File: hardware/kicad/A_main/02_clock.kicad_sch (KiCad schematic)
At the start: 29 parts, among them U15 ADCLK846BCPZ, U16 SN65LVDS2DBVR, U17 SN65LVDS2DBVR, U18 SN65LVDS2DBVR, Y10 ABLNO-V-80.000MHZ

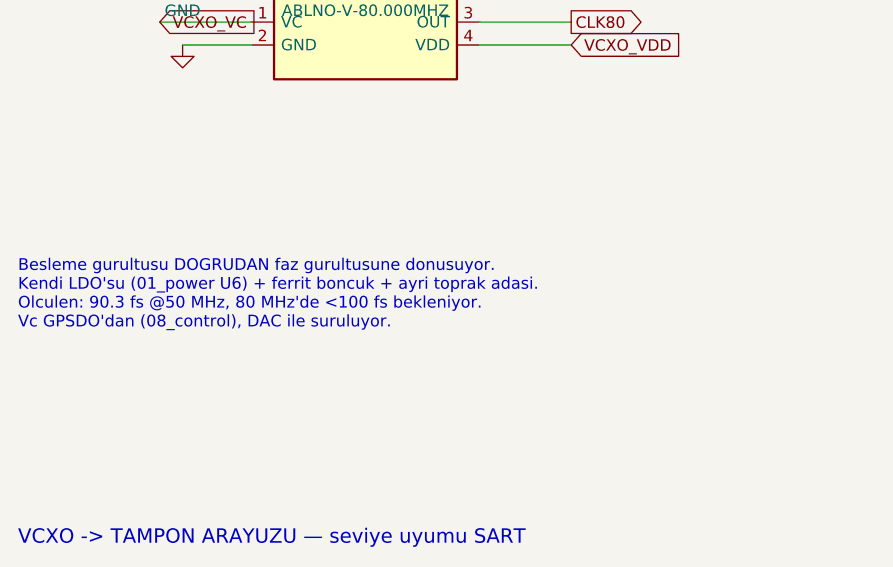
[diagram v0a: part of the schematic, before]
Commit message: Name the copyright holder and stamp it into the generated files
The repository had three licence files and no statement of who owns
the work. The only record of authorship was the git author field.

Copyleft depends on that statement. GPL and CERN-OHL-S work because
the holder grants permission on condition of reciprocity; with no
holder named there is nobody to require it from a downstream user.
Naming the author keeps the design open rather than closing it.

kicad/telif.py is the single source. The line reaches the schematics
through their title block and not through the generators, because
every schematic file is rewritten on each build and a header placed in
a generator would disappear at the first regeneration. All 23
schematics carry it. 109 source files have SPDX headers, split by the
project's own table: generators and the layout chain are hardware
under CERN-OHL-S-2.0, HDL and the audit tools are software under
GPL-3.0-only.

Board C's inductors also move to footprints that match parts that can
be bought. All of them sat on 0805 pads. Of the values this design
needs, 33 to 220 nH are 0603 parts, 470 and 820 nH are 0805, and
everything from 1000 nH upward is 1210, which is 3.2 by 2.5 mm and
does not fit an 0805 land. 32 inductors could not have been soldered.

A symbol-against-footprint check cannot find this. Those two agreed
with each other; what was wrong was the body size of the real part
behind the footprint.
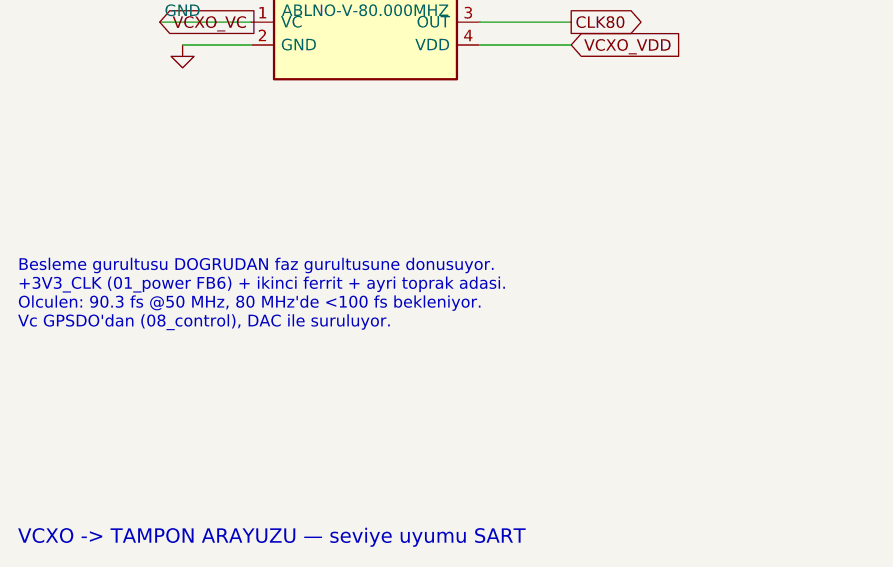
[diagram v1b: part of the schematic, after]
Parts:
- removed C210 (x2), C211 (x2): 100nF, Capacitor_SMD:C_0603_1608Metric, symbol Device:C
- added C210 (x2), C211 (x2): 100nF, Capacitor_SMD:C_0603_1608Metric, symbol Device:C
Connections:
- net +3V3: now also C210.1, C211.1
- net BUFCLK_N: now also C211.1
- net BUFCLK_P: now also C210.2
- net CLK80_DIV: now also C210.1
- net GND: now also C210.2, C211.2, C211.2
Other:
- note added: "Besleme gurultusu DOGRUDAN faz gurultusune donusuyor. +3V3_CLK (01_power FB6) + ikinci ferrit + ayri toprak adasi. Olculen: 90.3 fs @50 MHz, 80 MHz'de <100 fs bekleniyor. Vc GPSDO'dan (08_control), DAC ile suruluyor."
- note removed: "Besleme gurultusu DOGRUDAN faz gurultusune donusuyor. Kendi LDO'su (01_power U6) + ferrit boncuk + ayri toprak adasi. Olculen: 90.3 fs @50 MHz, 80 MHz'de <100 fs bekleniyor. Vc GPSDO'dan (08_control), DAC ile suruluyor."

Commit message: Correct the transmit envelope and add a third zero on 15 m to 10 m
The unit has no reconstruction filter. A comment on board A said that
the filter is on board C. Board C has no such filter: the transmit
signal enters through an SMA connector and goes to the transmit and
receive relay. The datasheet also gave a cutoff frequency for this
filter that does not exist.

A sampling DAC does not make one frequency. It makes images at
|k*fs +/- fd|. The zero-order hold gives each image a different
level, and the function falls slowly. If the carrier is near Nyquist,
an image at a lower frequency can be stronger than the carrier.

A new tool measures this. It uses the harmonic filter of board D,
because that filter is the only one in the transmit path.

  15 m to 10 m   4-channel   image at 10.3 MHz is 10.4 dB stronger
  6 m            4-channel   image is 14.2 dB stronger
  6 m            2-channel   image is 7.4 dB stronger
  20 m, 17 m     4-channel   -12.0 dBc, the limit is -43 dBc
  15 m to 10 m   2-channel   -40.4 dBc, the limit is -43 dBc

Only the last one is correctable.

That filter position must attenuate three frequencies: 42 MHz (the
second harmonic of 21 MHz), 63 MHz (the third harmonic) and 50.3 MHz
(the DAC image). A five-pole filter has two traps. No pair of trap
frequencies gives more than 1.9 dB of margin, and 1.9 dB is not a
margin: one E24 rounding already cost 19 dB in this project.

A shunt series-LC at the output adds a third zero. The image goes
from -40.4 dBc to -47.3 dBc, and the margin becomes 23 dB. Above
resonance the branch is capacitive and attenuates the whole stopband,
so the harmonics also improve. The passband loss falls from 1.35 dB
to 0.99 dB.

The transmit envelope is now written honestly. The RTL said "Nyquist
is 20 MHz, so 160 m to 17 m". Nyquist alone is not enough: the images
must also be filtered, and the real limit is lower.

  4-channel   160 m to 30 m
  2-channel   160 m to 10 m
  6 m         no transmit. Receive works, with 68 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
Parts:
- removed C210 (x2), C211 (x2): 100nF, Capacitor_SMD:C_0603_1608Metric, symbol Device:C
- added C210 (x2), C211 (x2): 100nF, Capacitor_SMD:C_0603_1608Metric, symbol Device:C
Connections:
- net +3V3: now also C210.1, C211.1
- net BUFCLK_N: now also C211.1
- net BUFCLK_P: now also C210.2
- net CLK80_DIV: now also C210.1
- net GND: now also C210.2, C211.2, C211.2

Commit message: Add bulk capacitors to the 1.8 V rails and measure the supply network
Counting decoupling capacitors is not enough. The existing check asks
whether each supply pin has a capacitor. That is necessary but not
sufficient. What matters is the impedance that the chip sees on the
rail, against frequency. No connectivity check can see this: the
schematic is correct, the netlist is correct, the DRC is clean, and
the rail still rings.

The +1V8 rail and the +1V8_D rail had no bulk capacitor. The largest
part was 1 uF. The regulator loop holds the impedance low to about
100 kHz. The ceramics hold it above about 1 MHz. Between them there
was nothing. The peak impedance on +1V8 was 994 mohm against a target
of 360 mohm.

This result does not depend on an assumption. A rail with no bulk
capacitor is a gap whatever transient current you assume.

The +1V1 core rail was also marginal: 228 mohm against 183 mohm. In
the upper band the impedance comes from the mounting inductance
divided by the number of capacitors, not from the value. So the
number changed, not the value.

Added: 22 uF and 10 uF on +1V8, 10 uF on +1V8_D. The 100 nF count
went from 6 to 14 on +1V1 and from 4 to 8 on +1V8. All rails now pass
with margin.

Three errors in the tool were corrected. Each one would have reversed
the answer:

The sweep went to 1 GHz, and every rail failed with its peak at
987 MHz, the top of the sweep. That was not an anti-resonance. The
model has no die capacitance, so the impedance rose without limit.
The board is responsible to about 200 MHz.

The regulator was a fixed 100 nH inductor, and this made a sharp
false resonance at 0.4 MHz. A switching regulator holds its output
impedance low up to its own crossover. Above that the bulk capacitors
dominate, and they were already counted. The same thing was counted
twice.

The transient current of the ECP5 core was 1.5 A, and the tool asked
for 37 capacitors. That number came from the assumption. The
LFE5U-25F is a small FPGA and its core curren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
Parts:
- removed C210 (x2), C211 (x2): 100nF, Capacitor_SMD:C_0603_1608Metric, symbol Device:C
- added C210 (x2), C211 (x2): 100nF, Capacitor_SMD:C_0603_1608Metric, symbol Device:C
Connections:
- net +3V3: now also C210.1, C211.1
- net BUFCLK_N: now also C211.1
- net BUFCLK_P: now also C210.2
- net CLK80_DIV: now also C210.1
- net GND: now also C210.2, C211.2, C211.2
